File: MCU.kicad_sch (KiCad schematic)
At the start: 17 parts, among them J1 AVR-ISP-6, Q1 BC547, Q2 BC547, SW1 SW_Push, SW2 SW_Push, U2 ATtiny85-20P

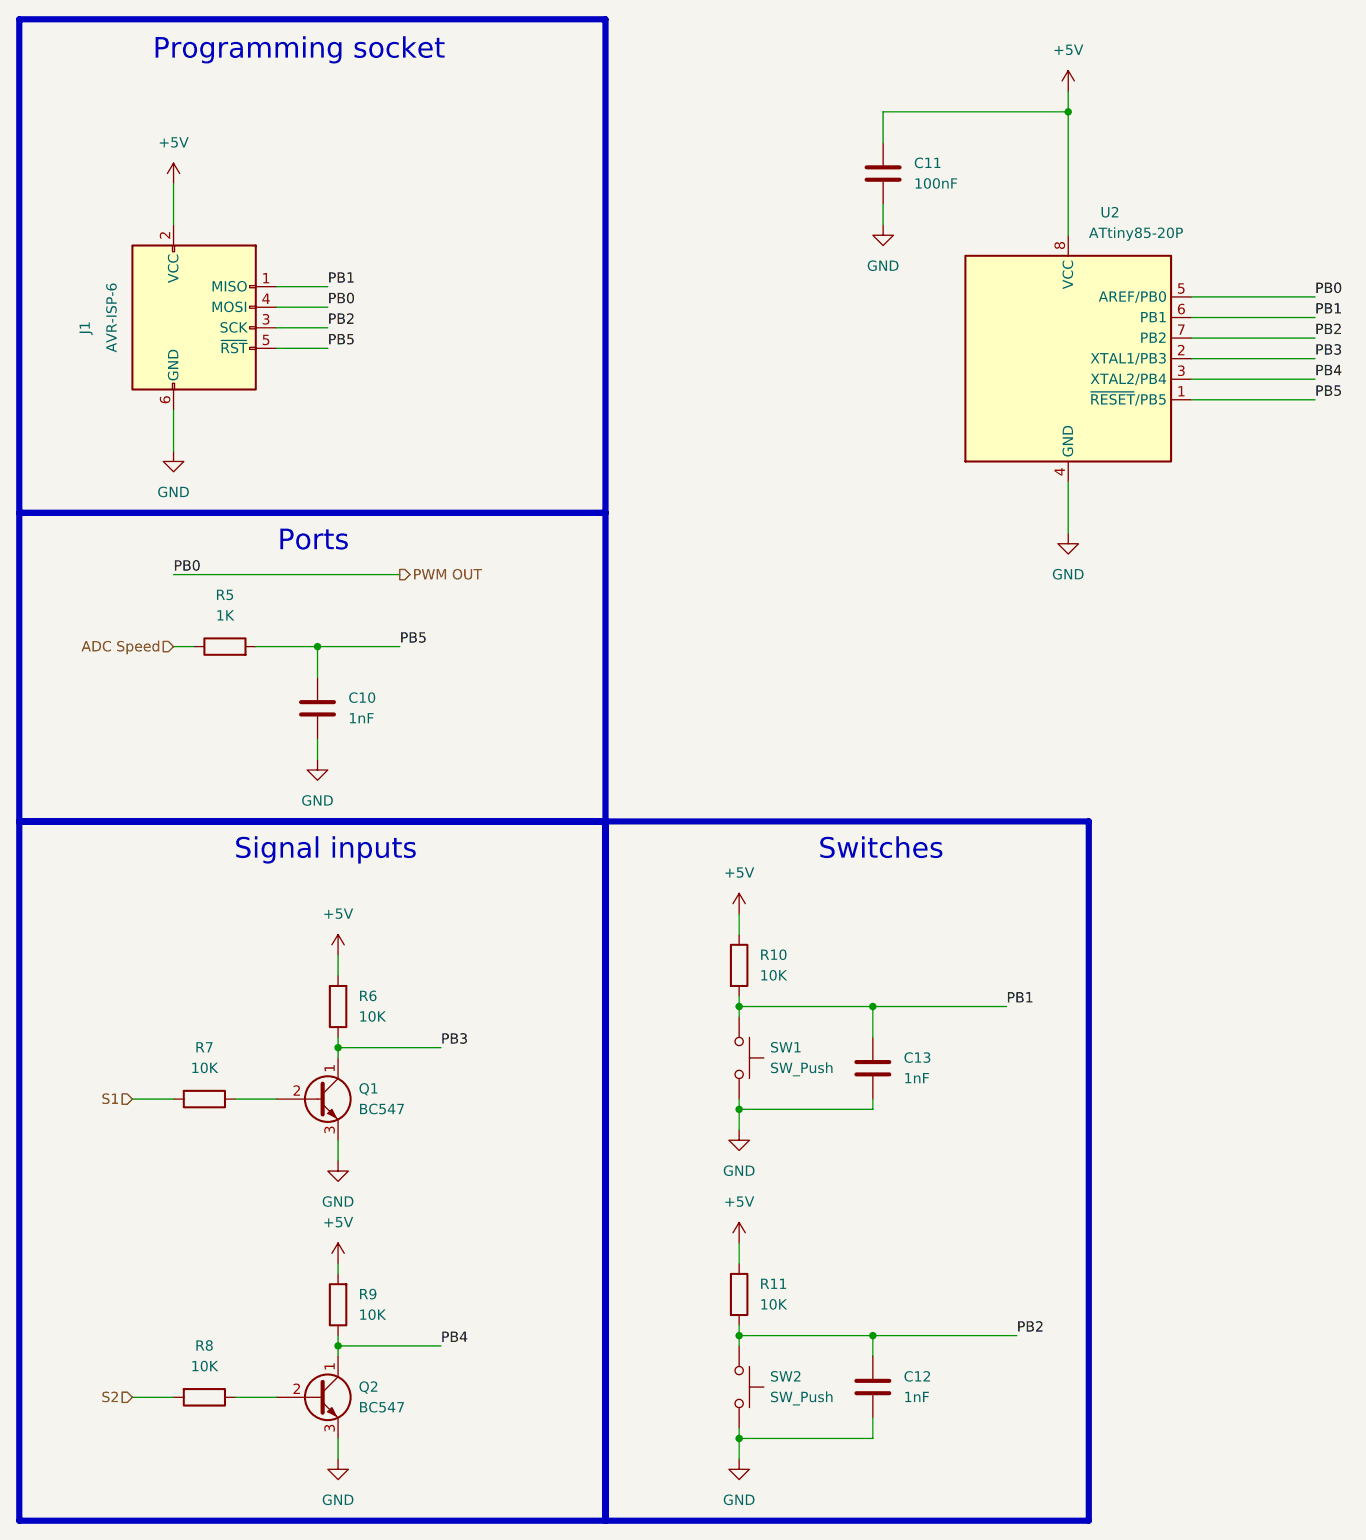
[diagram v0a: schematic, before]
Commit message: Correction in designators.
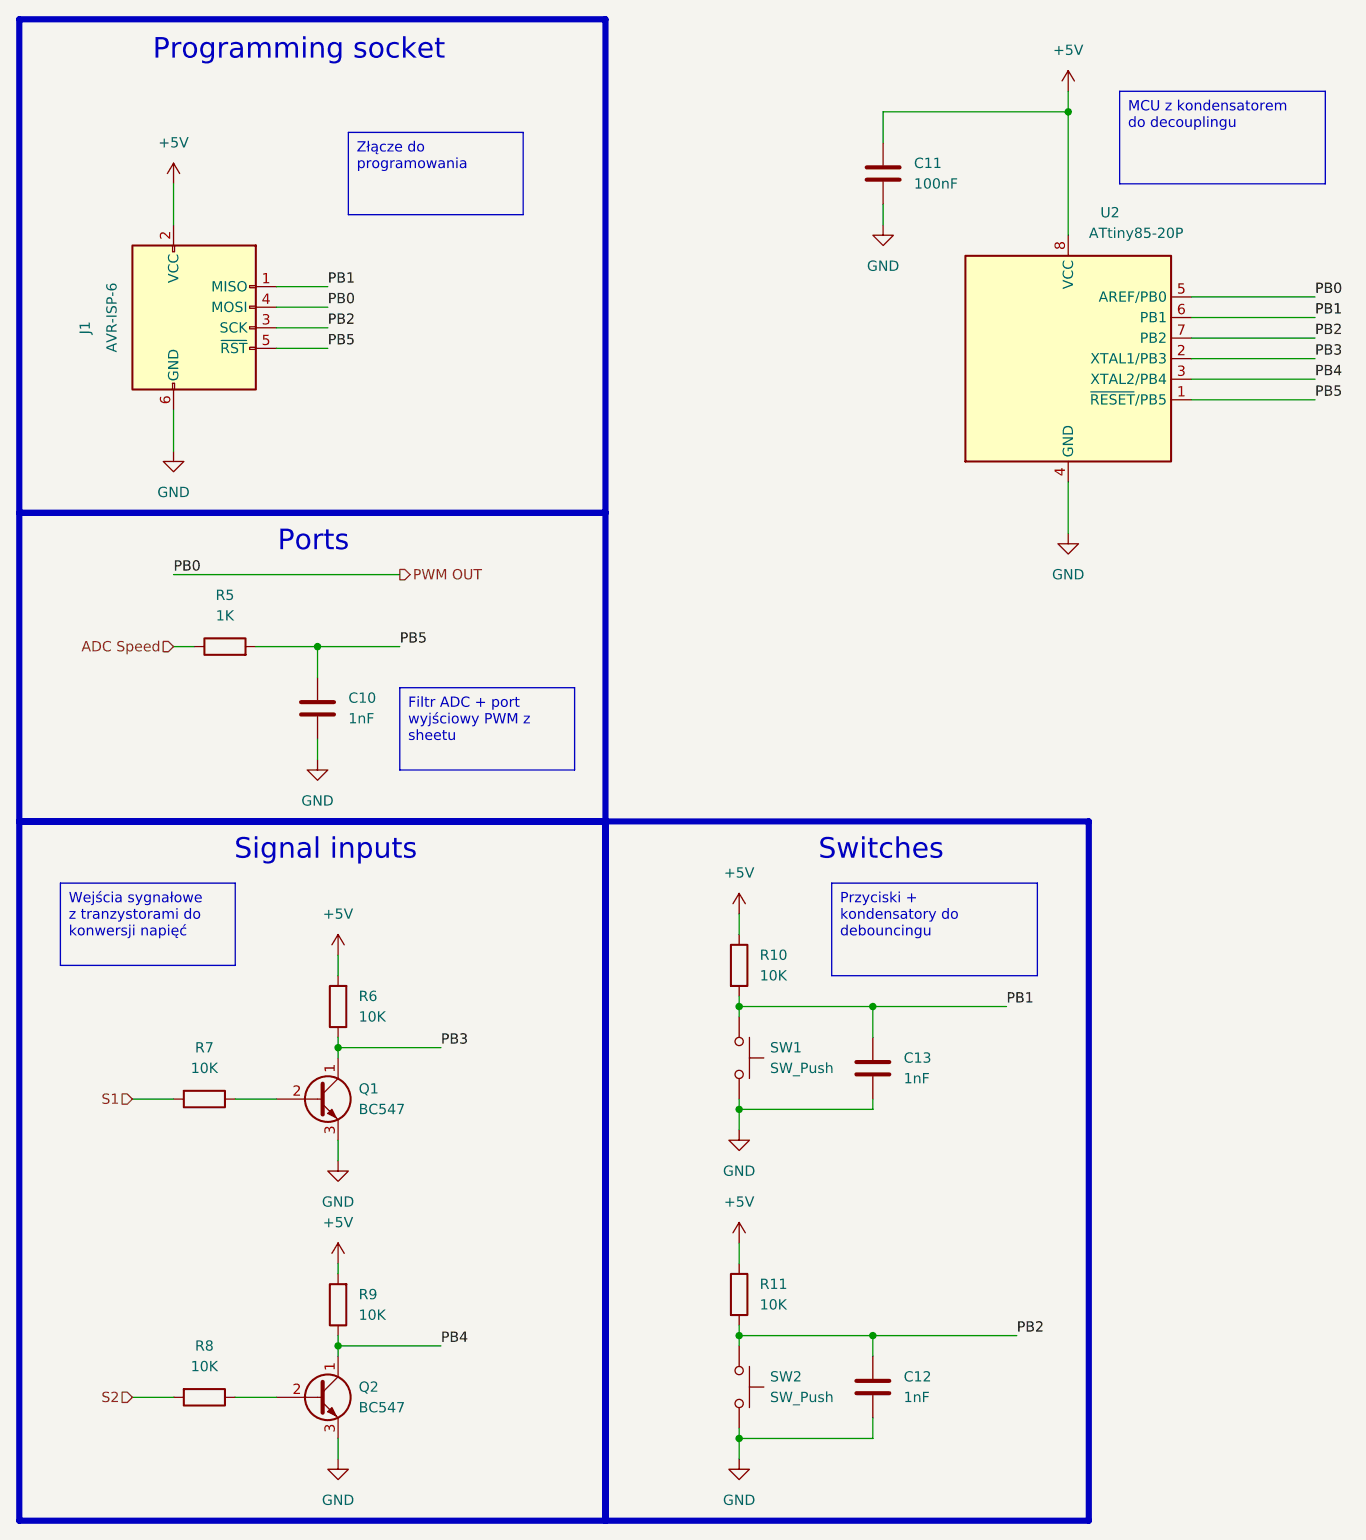
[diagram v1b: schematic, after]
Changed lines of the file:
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@@
+		)
+	)
+	(text_box "Wejścia sygnałowe z tranzystorami do konwersji napięć"
+		(exclude_from_sim no)
+		(at 17.78 119.38 0)
+		(size 21.59 10.16)
+		(stroke
+			(width 0)
+			(type default)
+		)
+		(fill
+			(type none)
+		)
+		(effects
+			(font
+				(size 1.27 1.27)
+			)
+			(justify left top)
+		)
+	)
+	(text_box "MCU z kondensatorem do decouplingu\n"
+		(exclude_from_sim no)
+		(at 148.59 21.59 0)
+		(size 25.4 11.43)
+		(stroke
+			(width 0)
+			(type default)
+		)
+		(fill
+			(type none)
+		)
+		(effects
+			(font
+				(size 1.27 1.27)
+			)
+			(justify left top)
+		)
+	)
+	(text_box "Przyciski + kondensatory do debouncingu\n\n"
+		(exclude_from_sim no)
+		(at 113.03 119.38 0)
+		(size 25.4 11.43)
+		(stroke
+			(width 0)
+			(type default)
+		)
+		(fill
+			(type none)
+		)
+		(effects
+			(font
+				(size 1.27 1.27)
+			)
+			(justify left top)
+		)
+	)
+	(text_box "Filtr ADC + port wyjściowy PWM z sheetu "
+		(exclude_from_sim no)
+		(at 59.69 95.25 0)
+		(size 21.59 10.16)
+		(stroke
+			(width 0)
+			(type default)
+		)
+		(fill
+			(type none)
+		)
+		(effects
+			(font
+				(size 1.27 1.27)
+			)
+			(justify left top)
+		)
+	)
+	(text_box "Złącze do programowania"
+		(exclude_from_sim no)
+		(at 53.34 26.67 0)
+		(size 21.59 10.16)
+		(stroke
+			(width 0)
+			(type default)
+		)
+		(fill
+			(type none)
+		)
+		(effects
+			(font
+				(size 1.27 1.27)
+			)
+			(justify left top)
 		)
 	)
